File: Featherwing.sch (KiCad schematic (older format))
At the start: 22 parts, among them J11 GS3, J2 CONN_01X16, J3 CONN_01X12, J5 GROVE-CONNECTOR-SMD-90D(4+2P-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, J9 CONN_01X06, U2 ROF-78E

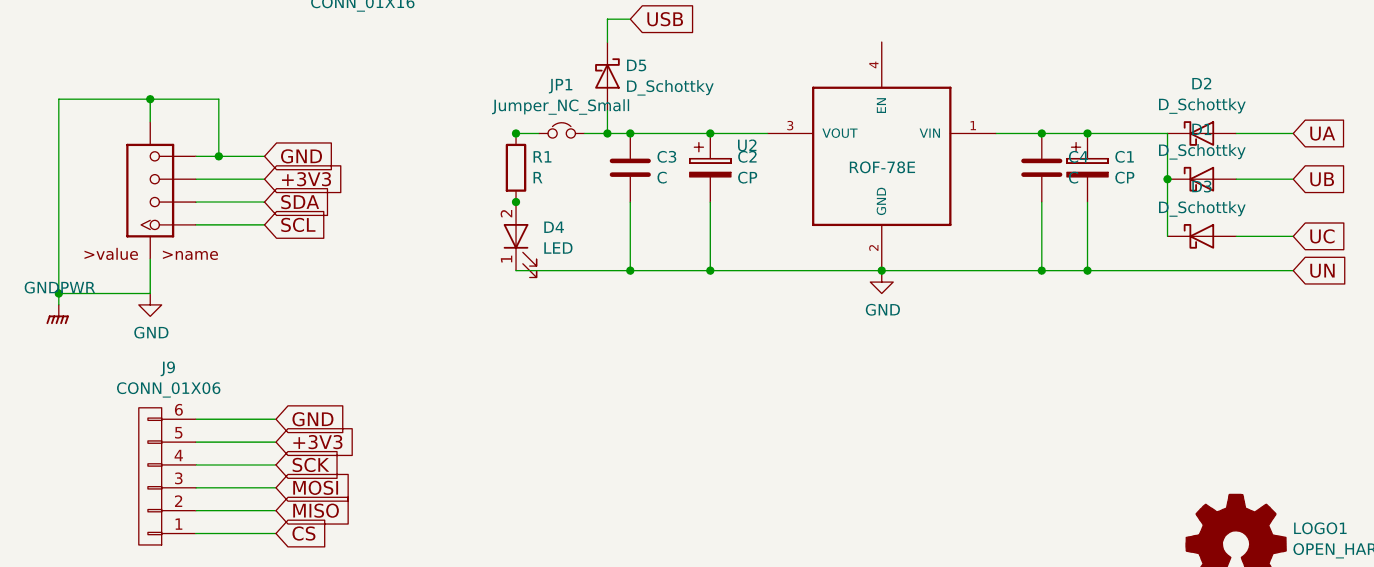
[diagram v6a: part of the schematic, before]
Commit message: Added component values from reference design
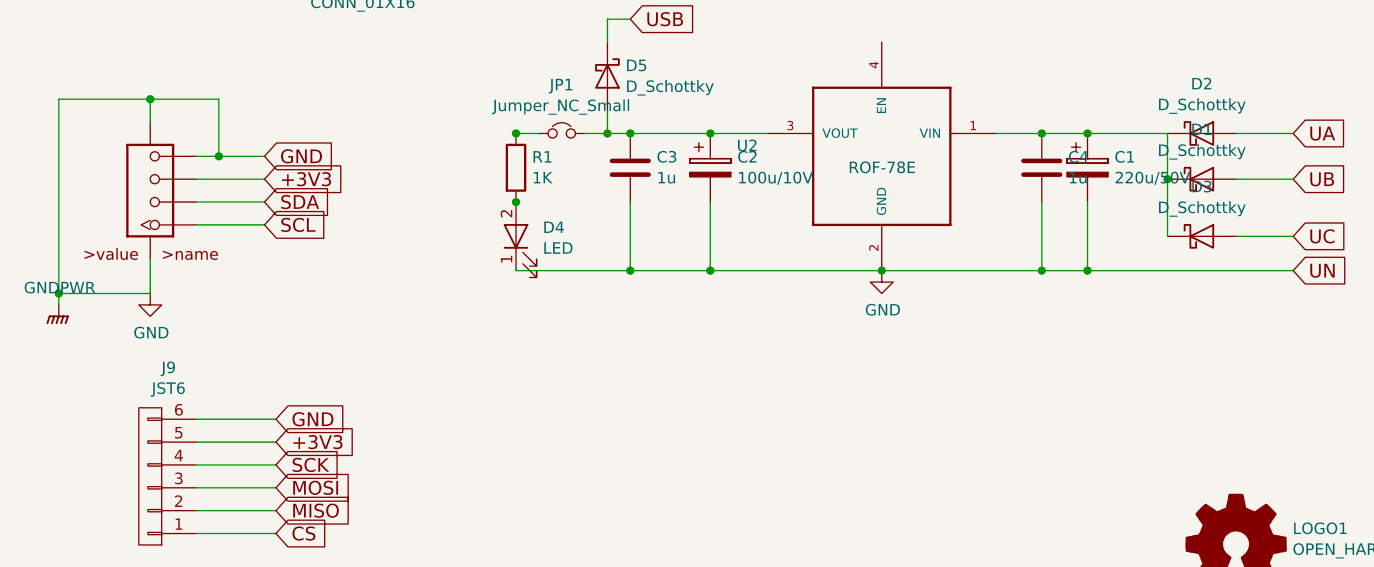
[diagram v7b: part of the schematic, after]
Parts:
- C1: value CP -> 220u/50V
- C2: value CP -> 100u/10V
- C3, C4: value C -> 1u
- D2: manf# (none) -> SS110
- J9: value CONN_01X06 -> JST6
- R1: value R -> 1K
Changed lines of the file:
@@
 F 2 "Diodes_SMD:D_SMA_Standard" H 100 -500 50  0001 C CNN
 F 3 "" H 100 -500 50  0001 C CNN
+F 4 "SS110" H 8200 2900 60  0001 C CNN "manf#"
 	1    8200 2900
 	1    0    0    -1
@@
 P 7700 3050
 F 0 "C1" H 7818 3096 50  0000 L CNN
-F 1 "CP" H 7818 3005 50  0000 L CNN
+F 1 "220u/50V" H 7818 3005 50  0000 L CNN
 F 2 "Capacitors_SMD:CP_Elec_8x10" H 288 -250 50  0001 C CNN
 F 3 "" H 250 -100 50  0001 C CNN
@@
 P 6050 3050
 F 0 "C2" H 6168 3096 50  0000 L CNN
-F 1 "CP" H 6168 3005 50  0000 L CNN
+F 1 "100u/10V" H 6168 3005 50  0000 L CNN
 F 2 "Capacitors_SMD:CP_Elec_5x5.8" H -1362 -250 50  0001 C CNN
 F 3 "" H -1400 -100 50  0001 C CNN
@@
 P 5700 3050
 F 0 "C3" H 5815 3096 50  0000 L CNN
-F 1 "C" H 5815 3005 50  0000 L CNN
+F 1 "1u" H 5815 3005 50  0000 L CNN
 F 2 "Capacitors_SMD:C_0603" H 288 0   50  0001 C CNN
 F 3 "" H 250 150 50  0001 C CNN
@@
 P 7500 3050
 F 0 "C4" H 7615 3096 50  0000 L CNN
-F 1 "C" H 7615 3005 50  0000 L CNN
+F 1 "1u" H 7615 3005 50  0000 L CNN
 F 2 "Capacitors_SMD:C_0603" H 2088 0   50  0001 C CNN
 F 3 "" H 2050 150 50  0001 C CNN
@@
 P 5200 3050
 F 0 "R1" H 5270 3096 50  0000 L CNN
-F 1 "R" H 5270 3005 50  0000 L CNN
+F 1 "1K" H 5270 3005 50  0000 L CNN
 F 2 "Resistors_SMD:R_0603_HandSoldering" V -70 150 50  0001 C CNN
 F 3 "" H 0   150 50  0001 C CNN
@@
 P 3600 4400
 F 0 "J9" H 3519 3925 50  0000 C CNN
-F 1 "CONN_01X06" H 3519 4016 50  0000 C CNN
+F 1 "JST6" H 3519 4016 50  0000 C CNN
 F 2 "Connectors_JST:JST_SH_SM06B-SRSS-TB_06x1.00mm_Angled" H 0   -150 50  0001 C CNN
 F 3 "" H 0   -150 50  0001 C CNN

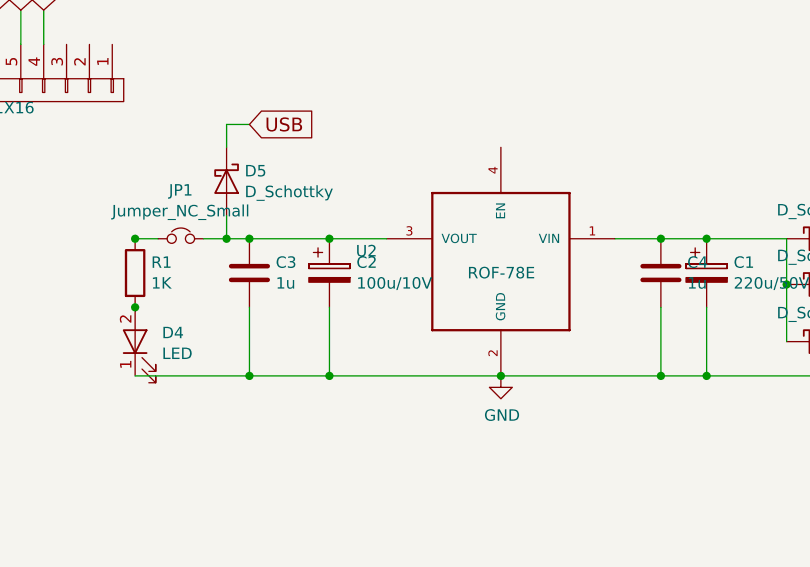
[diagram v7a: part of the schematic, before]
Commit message: Started adding part numbers
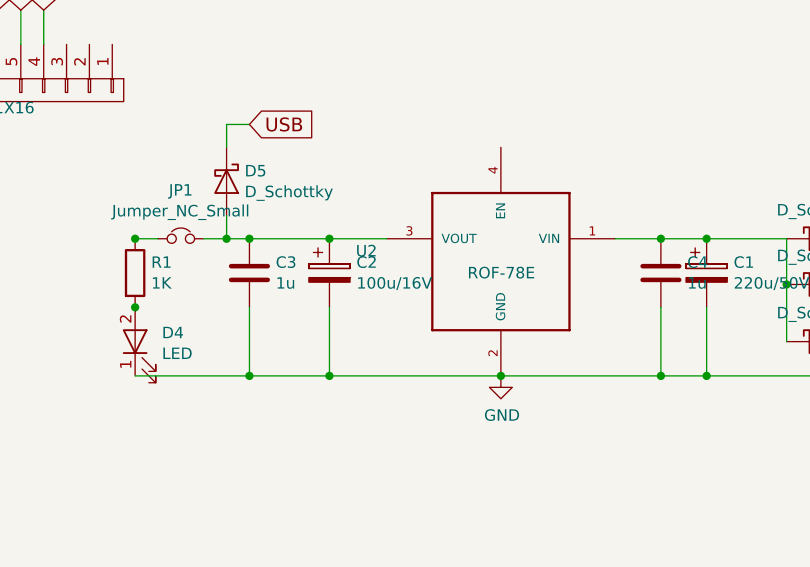
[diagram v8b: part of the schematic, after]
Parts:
- C2: value 100u/10V -> 100u/16V; manf# (none) -> EEEFT1C101AR
- D5: manf# (none) -> PMEG2010ER
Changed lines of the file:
@@
 P 6050 3050
 F 0 "C2" H 6168 3096 50  0000 L CNN
-F 1 "100u/10V" H 6168 3005 50  0000 L CNN
+F 1 "100u/16V" H 6168 3005 50  0000 L CNN
 F 2 "Capacitors_SMD:CP_Elec_5x5.8" H -1362 -250 50  0001 C CNN
 F 3 "" H -1400 -100 50  0001 C CNN
+F 4 "EEEFT1C101AR" H 6050 3050 60  0001 C CNN "manf#"
 	1    6050 3050
 	1    0    0    -1
@@
 F 2 "Diodes_SMD:D_SOD-123" H 50  -50 50  0001 C CNN
 F 3 "" H 50  -50 50  0001 C CNN
+F 4 "PMEG2010ER" H 5600 2650 60  0001 C CNN "manf#"
 	1    5600 2650
 	0    1    1    0
